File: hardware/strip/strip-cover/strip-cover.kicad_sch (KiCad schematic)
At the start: 7 parts

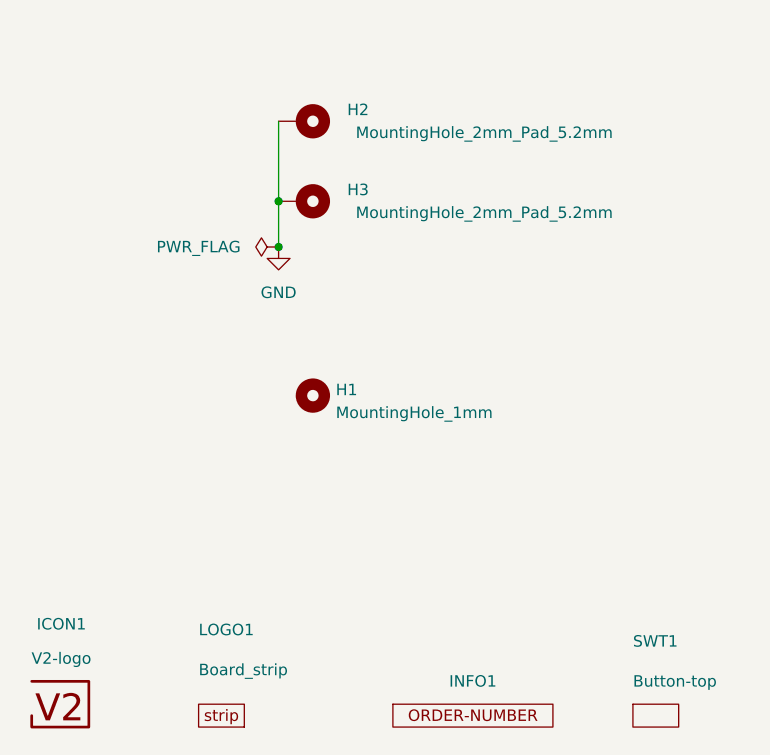
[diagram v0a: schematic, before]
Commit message: Replace Order_Number
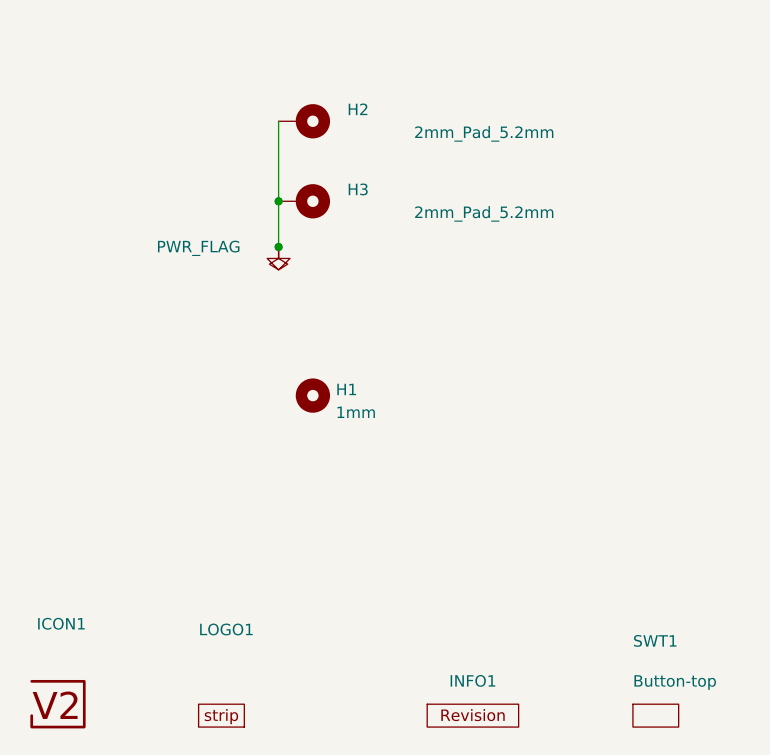
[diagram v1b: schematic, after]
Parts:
- H1: value MountingHole_1mm -> 1mm
- H2, H3: value MountingHole_2mm_Pad_5.2mm -> 2mm_Pad_5.2mm
- INFO1: value Order_Number -> (none); footprint V2_Production:Order_Number -> V2_Production:Revision; symbol V2_Production:Order_Number -> V2_Production:Revision
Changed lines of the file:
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@@
 (kicad_sch
-	(version 20231120)
+	(version 20250114)
 	(generator "eeschema")
-	(generator_version "8.0")
+	(generator_version "9.0")
 	(paper "A4")
 	(title_block
 		(title "V2 strip")
-		(date "2023-09-12")
-		(rev "2")
+		(date "2026-02-13")
+		(rev "2026-02-13")
 		(company "Versio Duo")
 		(comment 1 "cover")
@@
 		(at 140.97 133.35 0)
 		(unit 1)
-		(exclude_from_sim yes)
+		(exclude_from_sim no)
 		(in_bom no)
 		(on_board yes)
@@
 				)
 				(justify left)
+				(hide yes)
 			)
 		)
@@
 			)
 		)
+		(property "Sim.Enable" "0"
+			(at 140.97 133.35 0)
+			(effects
+				(font
+					(size 1.27 1.27)
+				)
+				(hide yes)
+			)
+		)
 		(instances
 			(project "strip-cover"
@@
 	)
 	(symbol
-		(lib_id "power:GND")
+		(lib_id "V2_power:GND")
 		(at 147.32 81.28 0)
 		(unit 1)
@@
 					(size 1.27 1.27)
 				)
+				(hide yes)
 			)
 		)
@@
 	)
 	(symbol
-		(lib_id "V2_Production:Order_Number")
+		(lib_id "V2_Production:Revision")
 		(at 168.91 133.35 0)
 		(unit 1)
-		(exclude_from_sim yes)
+		(exclude_from_sim no)
 		(in_bom no)
 		(on_board yes)
@@
 			)
 		)
-		(property "Value" "Order_Number"
+		(property "Value" ""
 			(at 168.91 135.89 0)
 			(effects
@@
 			)
 		)
-		(property "Footprint" "V2_Production:Order_Number"
+		(property "Footprint" "V2_Production:Revision"
 			(at 168.91 138.43 0)
 			(effects
@@
 		(at 189.23 133.35 0)
 		(unit 1)
-		(exclude_from_sim yes)
+		(exclude_from_sim no)
 		(in_bom no)
 		(on_board yes)
@@
 			)
 		)
+		(property "Sim.Enable" "0"
+			(at 189.23 133.35 0)
+			(effects
+				(font
+					(size 1.27 1.27)
+				)
+				(hide yes)
+			)
+		)
 		(instances
 			(project "strip-cover"
@@
 		(at 149.86 67.31 270)
 		(unit 1)
-		(exclude_from_sim yes)
+		(exclude_from_sim no)
 		(in_bom no)
 		(on_board yes)
@@
 			)
 		)
-		(property "Value" "MountingHole_2mm_Pad_5.2mm"
+		(property "Value" "2mm_Pad_5.2mm"
 			(at 170.18 68.58 90)
 			(effects
@@
 			)
 		)
-		(property "Datasheet" "~"
+		(property "Datasheet" ""
 			(at 149.86 67.31 0)
 			(effects
@@
 			)
 		)
-		(property "Description" ""
+		(property "Description" "Mounting Hole with connection"
 			(at 149.86 67.31 0)
 			(effects
@@
 	)
 	(symbol
-		(lib_id "power:PWR_FLAG")
+		(lib_id "V2_power:PWR_FLAG")
 		(at 147.32 81.28 90)
 		(unit 1)
@@
 			)
 		)
-		(property "Datasheet" "~"
+		(property "Datasheet" ""
 			(at 147.32 81.28 0)
 			(effects
@@
 			)
 		)
-		(property "Description" ""
+		(property "Description" "Special symbol for telling ERC where power comes from"
 			(at 147.32 81.28 0)
 			(effects
@@
 		(at 151.13 97.79 0)
 		(unit 1)
-		(exclude_from_sim yes)
+		(exclude_from_sim no)
 		(in_bom no)
 		(on_board yes)
@@
 			)
 		)
-		(property "Value" "MountingHole_1mm"
+		(property "Value" "1mm"
 			(at 153.67 99.695 0)
 			(effects
@@
 			)
 		)
-		(property "Datasheet" "~"
+		(property "Datasheet" ""
 			(at 151.13 97.79 0)
 			(effects
@@
 			)
 		)
-		(property "Description" ""
+		(property "Description" "Mounting Hole without connection"
 			(at 151.13 97.79 0)
 			(effects
@@
 		(at 123.19 132.08 0)
 		(unit 1)
-		(exclude_from_sim yes)
+		(exclude_from_sim no)
 		(in_bom no)
 		(on_board yes)
@@
 					(size 1.27 1.27)
 				)
+				(hide yes)
 			)
 		)
@@
 		(at 149.86 76.2 270)
 		(unit 1)
-		(exclude_from_sim yes)
+		(exclude_from_sim no)
 		(in_bom no)
 		(on_board yes)
@@
 			)
 		)
-		(property "Value" "MountingHole_2mm_Pad_5.2mm"
+		(property "Value" "2mm_Pad_5.2mm"
 			(at 170.18 77.47 90)
 			(effects
@@
 			)
 		)
-		(property "Datasheet" "~"
+		(property "Datasheet" ""
 			(at 149.86 76.2 0)
 			(effects
@@
 			)
 		)
-		(property "Description" ""
+		(property "Description" "Mounting Hole with connection"
 			(at 149.86 76.2 0)
 			(effects
@@
 		)
 	)
+	(embedded_fonts no)
 )

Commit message: Update Library
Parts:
- INFO1: value (none) -> ~
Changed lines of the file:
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@@
-	)
-	(junction
-		(at 147.32 81.28)
-		(diameter 0)
-		(color 0 0 0 0)
 	)
 	(junction
@@
 		(at 140.97 133.35 0)
 		(unit 1)
-		(exclude_from_sim no)
+		(exclude_from_sim yes)
 		(in_bom no)
 		(on_board yes)
@@
 		)
 		(property "Description" ""
-			(at 140.97 133.35 0)
-			(effects
-				(font
-					(size 1.27 1.27)
-				)
-				(hide yes)
-			)
-		)
-		(property "Sim.Enable" "0"
 			(at 140.97 133.35 0)
 			(effects
@@
 			)
 		)
-		(property "Value" ""
+		(property "Value" "~"
 			(at 168.91 135.89 0)
 			(effects
@@
 		(at 189.23 133.35 0)
 		(unit 1)
+		(exclude_from_sim yes)
+		(in_bom no)
+		(on_board yes)
+		(dnp no)
+		(property "Reference" "SWT1"
+			(at 186.69 125.0949 0)
+			(effects
+				(font
+					(size 1.27 1.27)
+				)
+				(justify left)
+			)
+		)
+		(property "Value" "Button-top"
+			(at 186.69 129.5399 0)
+			(effects
+				(font
+					(size 1.27 1.27)
+				)
+				(justify left)
+			)
+		)
+		(property "Footprint" "V2_PCB_Devices:PCB_Button-top"
+			(at 189.23 138.43 0)
+			(effects
+				(font
+					(size 1.27 1.27)
+				)
+				(hide yes)
+			)
+		)
+		(property "Datasheet" ""
+			(at 189.23 133.35 0)
+			(effects
+				(font
+					(size 1.27 1.27)
+				)
+				(hide yes)
+			)
+		)
+		(property "Description" ""
+			(at 189.23 133.35 0)
+			(effects
+				(font
+					(size 1.27 1.27)
+				)
+				(hide yes)
+			)
+		)
+		(instances
+			(project "strip-cover"
+				(path "/6c8448b4-b04d-47e1-934e-e40cbe27a7be"
+					(reference "SWT1")
+					(unit 1)
+				)
+			)
+		)
+	)
+	(symbol
+		(lib_id "V2_Mechanical:MountingHole_2mm_Pad_5.2mm")
+		(at 149.86 67.31 270)
+		(unit 1)
 		(exclude_from_sim no)
 		(in_bom no)
 		(on_board yes)
 		(dnp no)
-		(property "Reference" "SWT1"
-			(at 186.69 125.0949 0)
-			(effects
-				(font
-					(size 1.27 1.27)
-				)
-				(justify left)
-			)
-		)
-		(property "Value" "Button-top"
-			(at 186.69 129.5399 0)
-			(effects
-				(font
-					(size 1.27 1.27)
-				)
-				(justify left)
-			)
-		)
-		(property "Footprint" "V2_PCB_Devices:PCB_Button-top"
-			(at 189.23 138.43 0)
-			(effects
-				(font
-					(size 1.27 1.27)
-				)
-				(hide yes)
-			)
-		)
-		(property "Datasheet" ""
-			(at 189.23 133.35 0)
-			(effects
-				(font
-					(size 1.27 1.27)
-				)
-				(hide yes)
-			)
-		)
-		(property "Description" ""
-			(at 189.23 133.35 0)
-			(effects
-				(font
-					(size 1.27 1.27)
-				)
-				(hide yes)
-			)
-		)
-		(property "Sim.Enable" "0"
-			(at 189.23 133.35 0)
-			(effects
-				(font
-					(size 1.27 1.27)
-				)
-				(hide yes)
-			)
-		)
-		(instances
-			(project "strip-cover"
-				(path "/6c8448b4-b04d-47e1-934e-e40cbe27a7be"
-					(reference "SWT1")
-					(unit 1)
-				)
-			)
-		)
-	)
-	(symbol
-		(lib_id "V2_Mechanical:MountingHole_2mm_Pad_5.2mm")
-		(at 149.86 67.31 270)
-		(unit 1)
-		(exclude_from_sim no)
-		(in_bom no)
-		(on_board yes)
-		(dnp no)
 		(property "Reference" "H2"
 			(at 154.94 66.04 90)
@@
 	)
 	(symbol
-		(lib_id "V2_power:PWR_FLAG")
-		(at 147.32 81.28 90)
+		(lib_id "V2_power:GND")
+		(at 157.48 57.15 90)
 		(unit 1)
 		(exclude_from_sim no)
@@
 		(on_board yes)
 		(dnp no)
+		(fields_autoplaced yes)
+		(property "Reference" "#PWR0102"
+			(at 163.83 57.15 0)
+			(effects
+				(font
+					(size 1.27 1.27)
+				)
+				(hide yes)
+			)
+		)
+		(property "Value" "GND"
+			(at 162.56 57.15 0)
+			(effects
+				(font
+					(size 1.27 1.27)
+				)
+				(hide yes)
+			)
+		)
+		(property "Footprint" ""
+			(at 157.48 57.15 0)
+			(effects
+				(font
+					(size 1.27 1.27)
+				)
+				(hide yes)
+			)
+		)
+		(property "Datasheet" ""
+			(at 157.48 57.15 0)
+			(effects
+				(font
+					(size 1.27 1.27)
+				)
+				(hide yes)
+			)
+		)
+		(property "Description" ""
+			(at 157.48 57.15 0)
+			(effects
+				(font
+					(size 1.27 1.27)
+				)
+				(hide yes)
+			)
+		)
+		(pin "1"
+		)
+		(instances
+			(project "strip-cover"
+				(path "/6c8448b4-b04d-47e1-934e-e40cbe27a7be"
+					(reference "#PWR0102")
+					(unit 1)
+				)
+			)
+		)
+	)
+	(symbol
+		(lib_id "V2_power:PWR_FLAG")
+		(at 157.48 57.15 0)
+		(unit 1)
+		(exclude_from_sim no)
+		(in_bom yes)
+		(on_board yes)
+		(dnp no)
 		(property "Reference" "#FLG0101"
-			(at 145.415 81.28 0)
+			(at 157.48 55.245 0)
 			(effects
 				(font
@@
 		)
 		(property "Value" "PWR_FLAG"
-			(at 138.43 81.28 90)
+			(at 147.828 57.15 0)
 			(effects
 				(font
@@
 		)
 		(property "Footprint" ""
-			(at 147.32 81.28 0)
-			(effects
-				(font
-					(size 1.27 1.27)
-				)
-				(hide yes)
-			)
-		)
-		(property "Datasheet" ""
-			(at 147.32 81.28 0)
+			(at 157.48 57.15 0)
+			(effects
+				(font
+					(size 1.27 1.27)
+				)
+				(hide yes)
+			)
+		)
+		(property "Datasheet" ""
+			(at 157.48 57.15 0)
 			(effects
 				(font
@@
 		)
 		(property "Description" "Special symbol for telling ERC where power comes from"
-			(at 147.32 81.28 0)
-			(effects
-				(font
+			(at 157.48 57.15 0)
+			(effects
+				(font

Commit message: Update
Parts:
- INFO1: value ~ -> (none)
